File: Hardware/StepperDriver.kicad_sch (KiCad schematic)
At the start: 60 parts, among them J1 DC, J2 MOTOR, J3 OLED, J4 JTAG, SW1 SPST_TS, SW2 SPST_TS, SW3 SPST_TS, U1 TPS5430DDA, U2 TMC2209-LA, U3 XIAO-ESP32C6

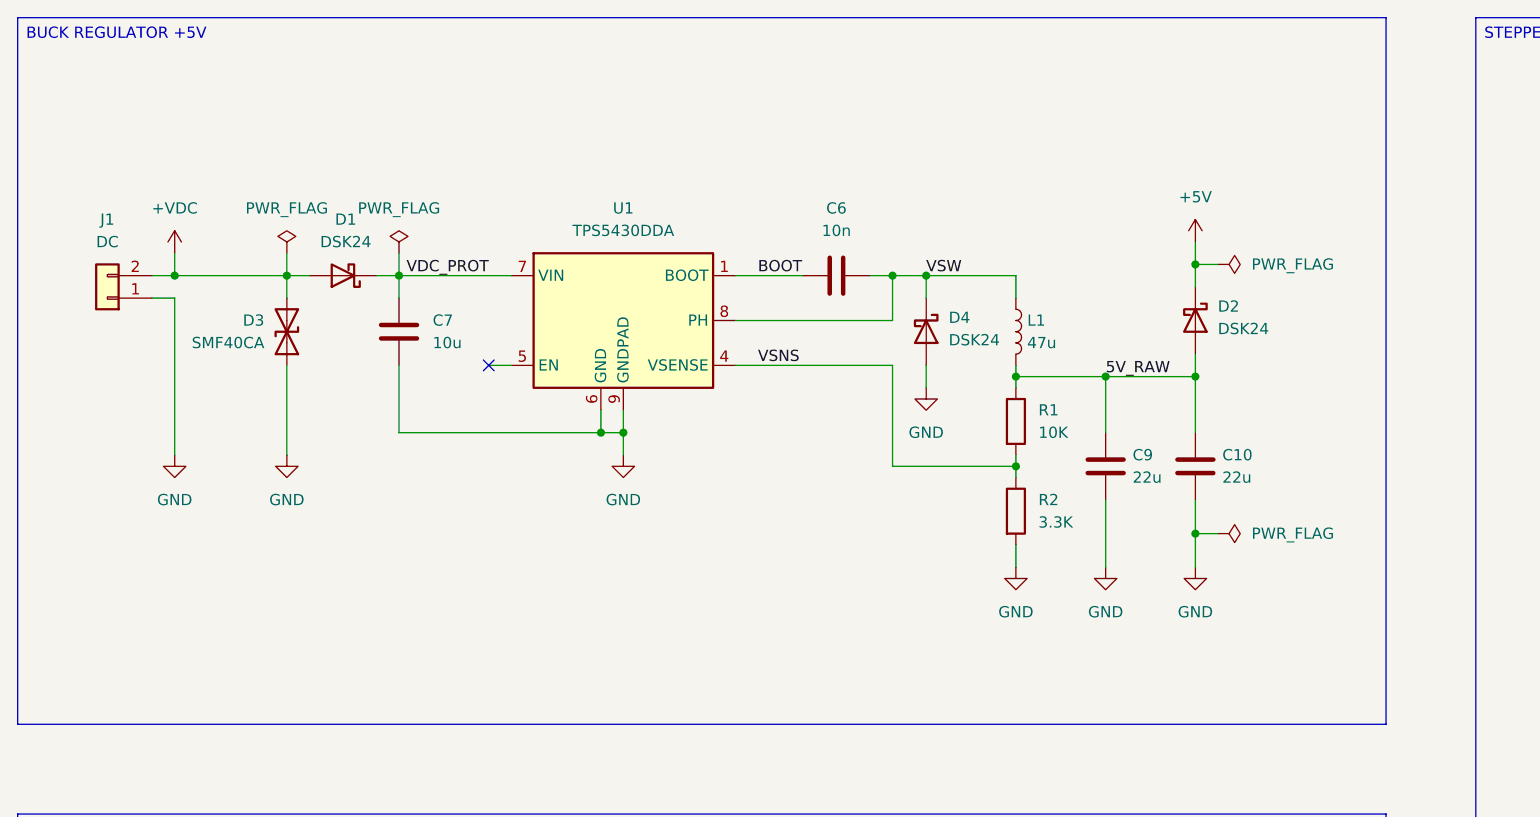
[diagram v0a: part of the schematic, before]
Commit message: Assembly review
Performed a full review of the schematic and layout.
Minor changes to the schematic and layout.
Updated output files.
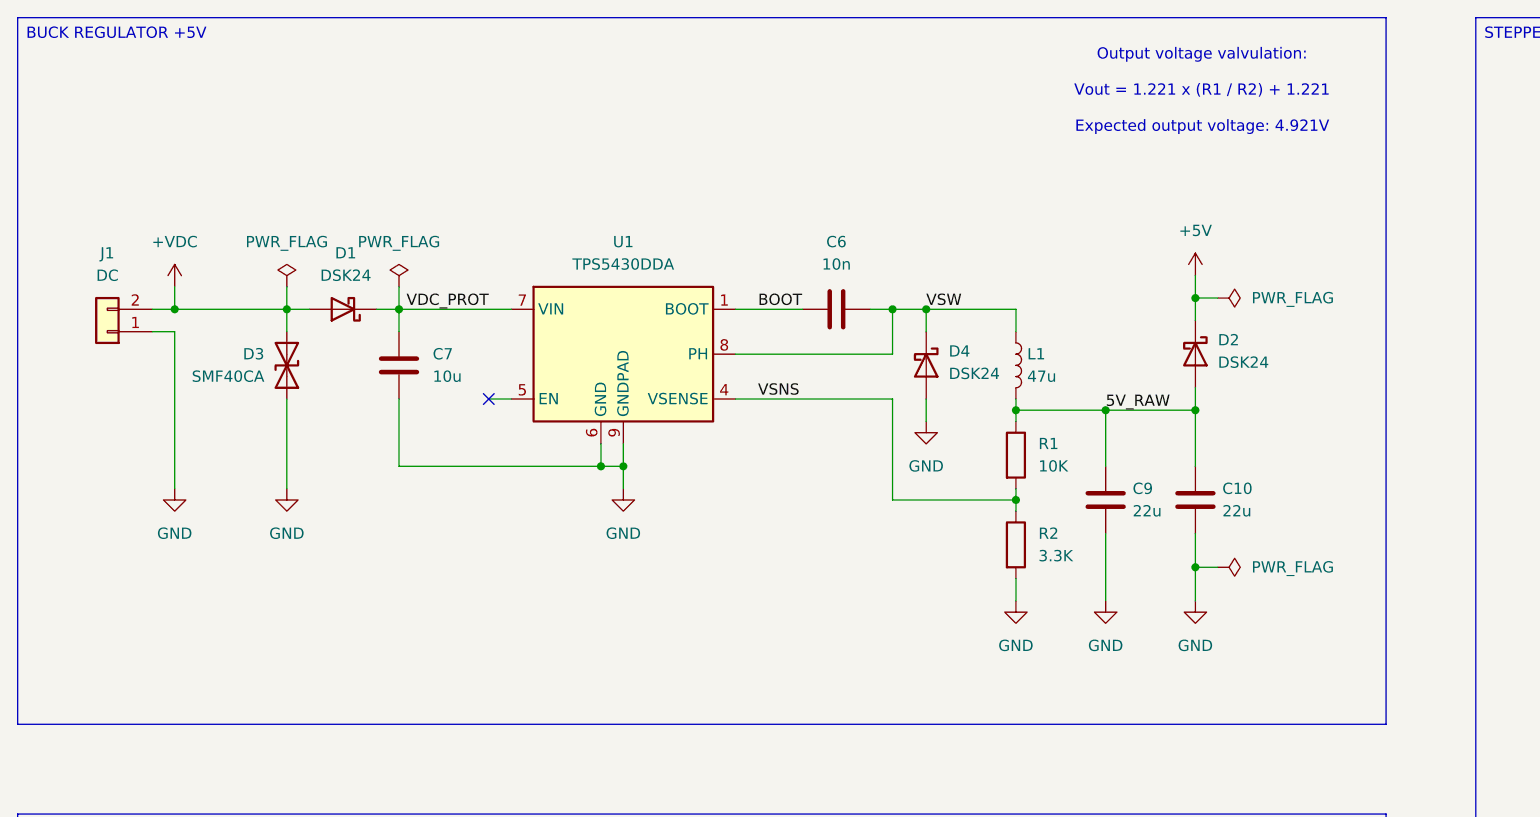
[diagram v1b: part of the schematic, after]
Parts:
- C4, C5: JLCPCB Part C5246552 -> C721322; Manufacturer Part HV1V476M0605PZ -> SVZ1VM470E06E00RAXXX
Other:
- note added: "Output voltage valvulation: Vout = 1.221 x (R1 / R2) + 1.221 Expected output voltage: 4.921V"
- moved on the sheet: C10, C6, C7, C9, D1, D2, D3, D4, J1, L1, R1, R2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
